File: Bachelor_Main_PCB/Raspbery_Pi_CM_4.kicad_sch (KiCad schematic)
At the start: 3 parts, among them U1 SC0683, X1 DF40HC_3.0_-100DS-0.4V_58, X2 DF40HC_3.0_-100DS-0.4V_58

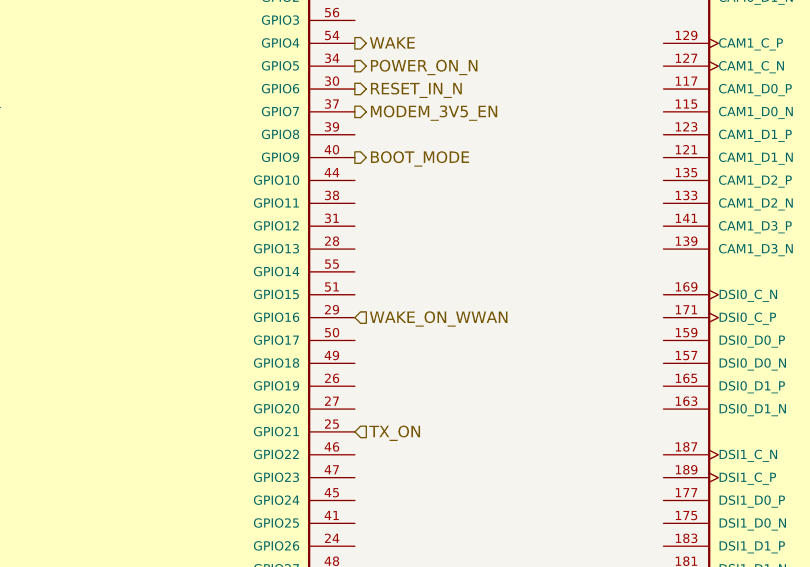
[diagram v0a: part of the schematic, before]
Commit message: Add RPI to MCU UART communication
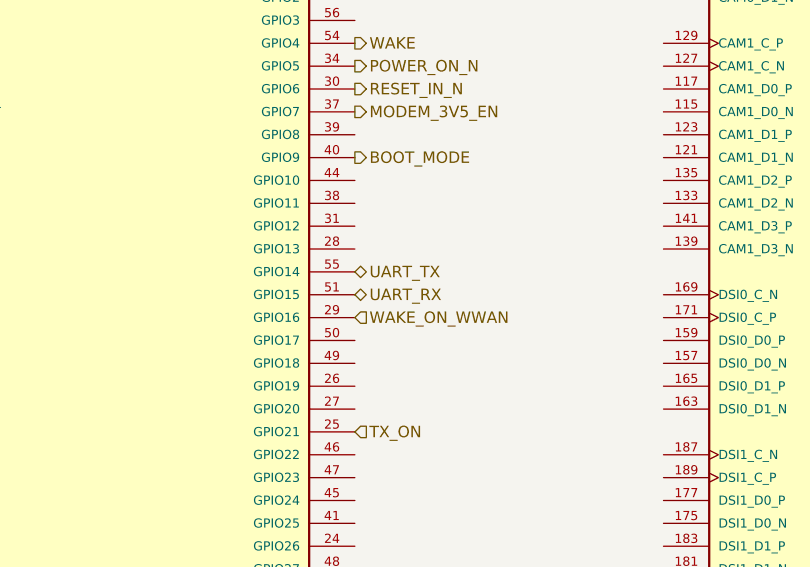
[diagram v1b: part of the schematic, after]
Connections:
- net UART_RX: now reaches U1.51 (GPIO15)
- net UART_TX: now reaches U1.55 (GPIO14)

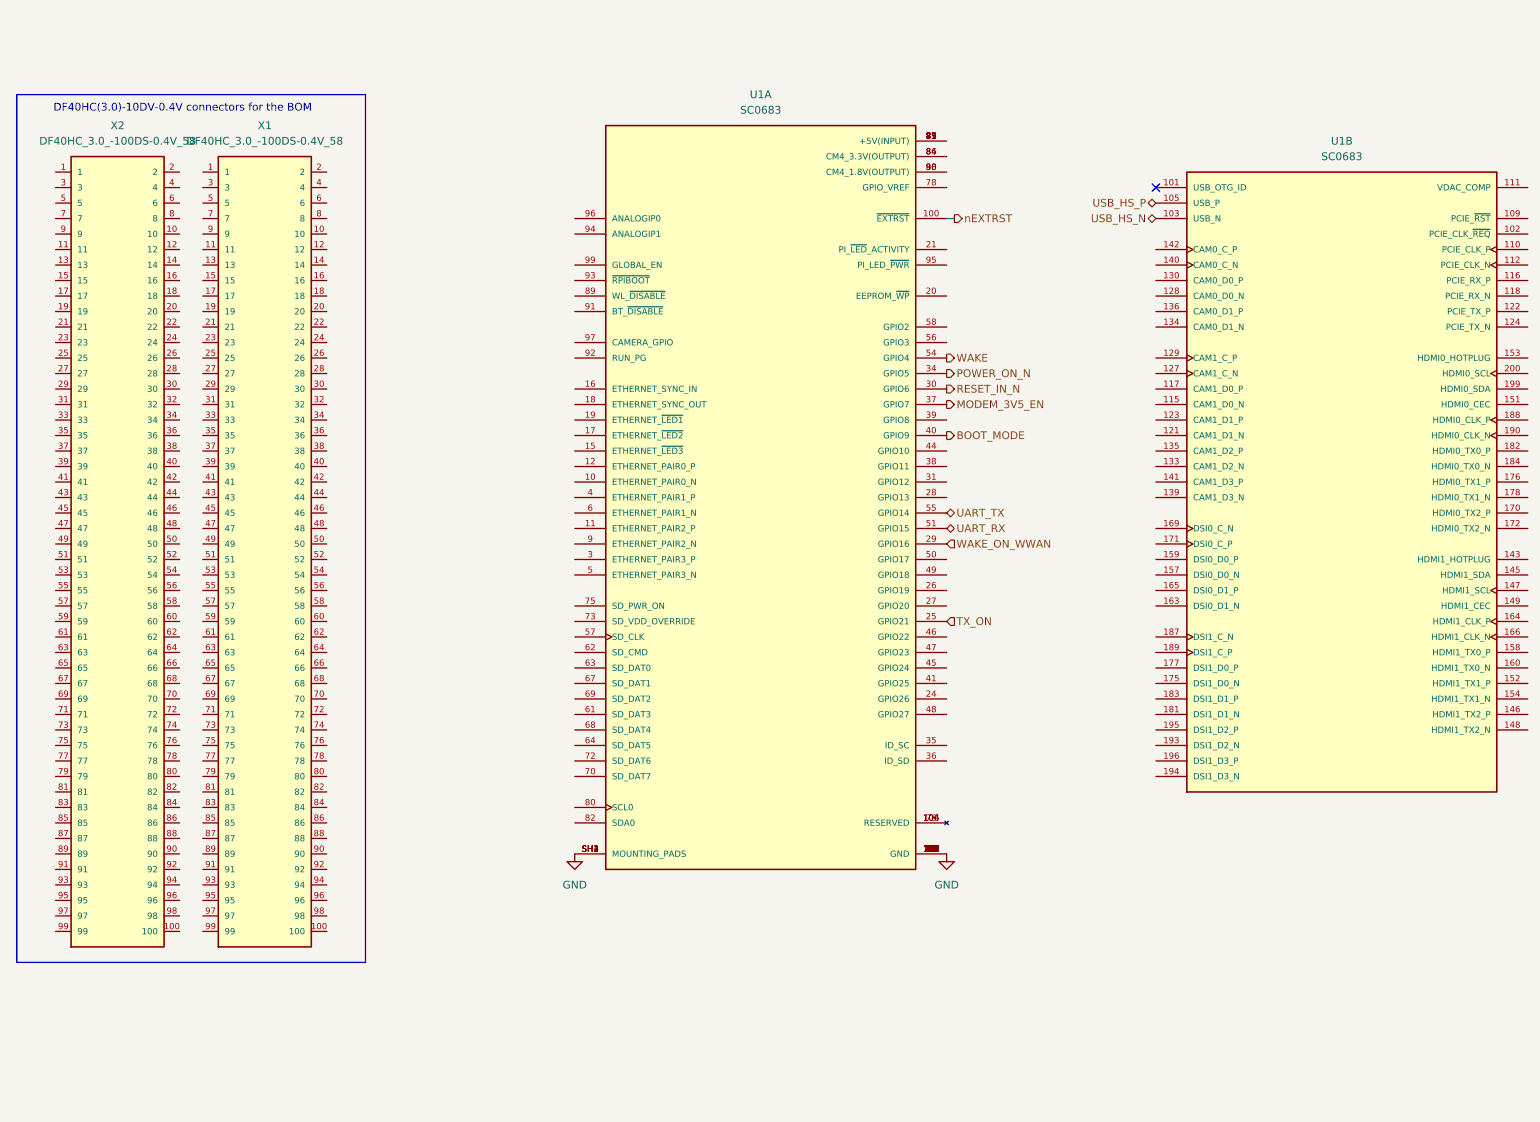
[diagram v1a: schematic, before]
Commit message: Add RPI power Switch MOSFET, Fix direction of power switch MOSFETs
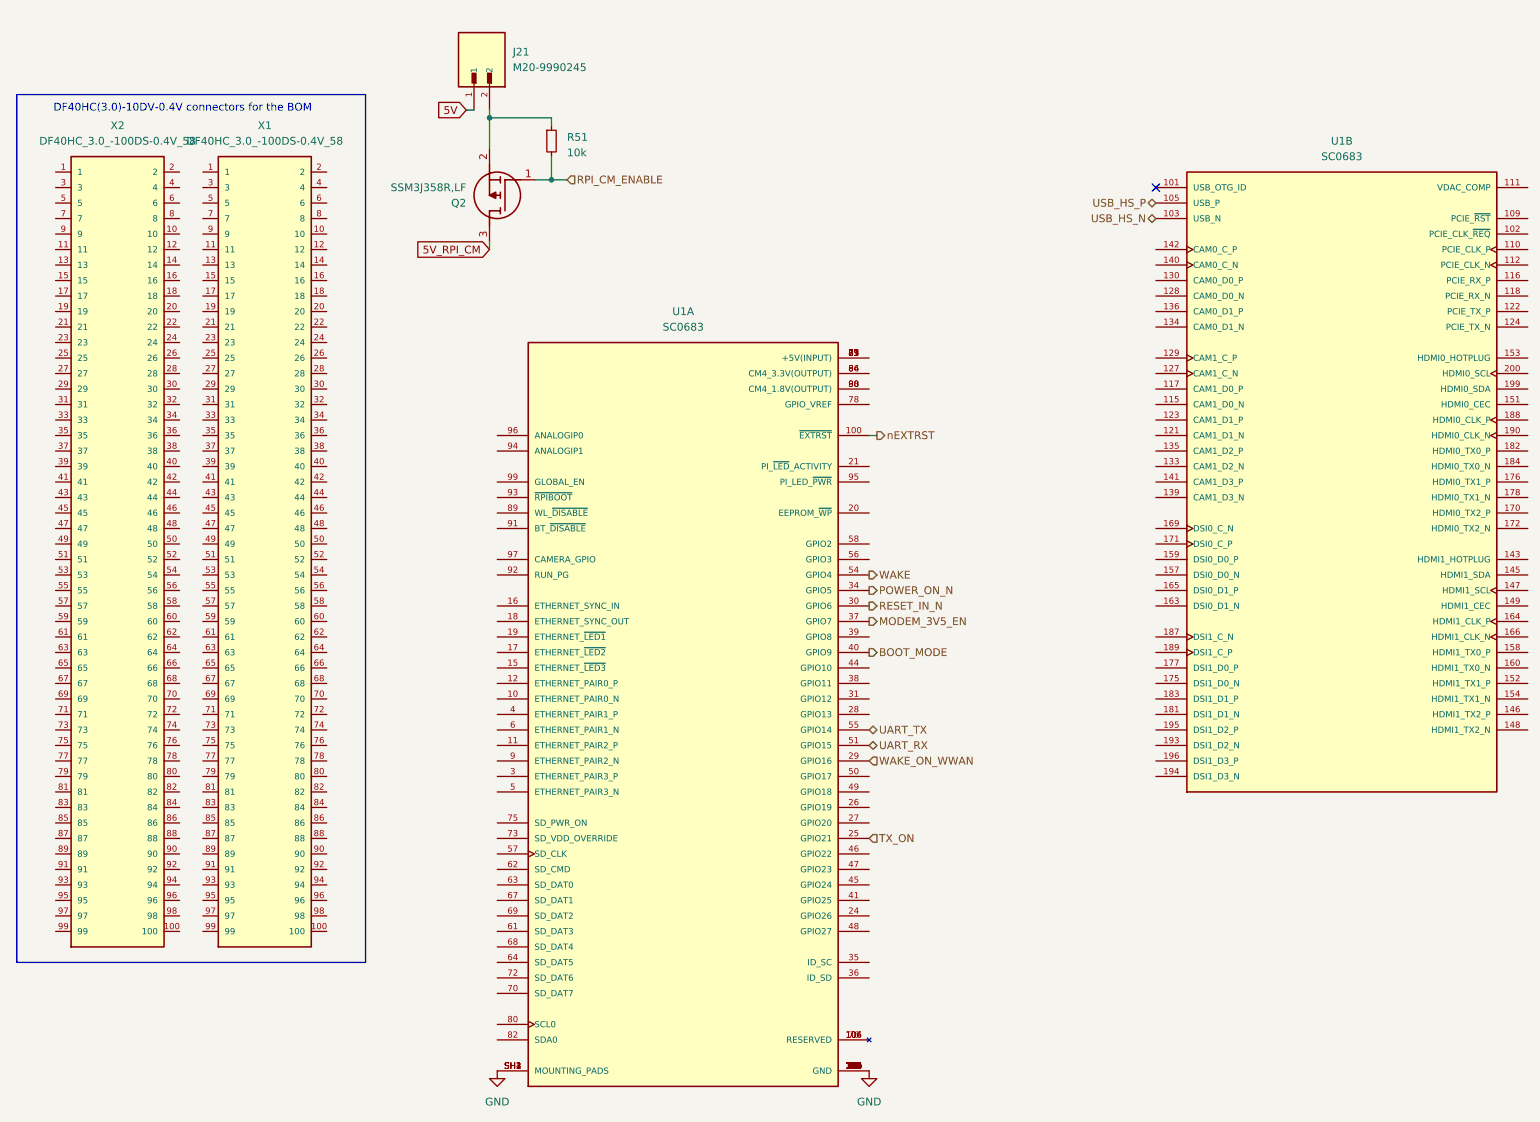
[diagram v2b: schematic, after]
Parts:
- added J21: M20-9990245, M20-9990245:HARWIN_M20-9990245, symbol M20-9990245:M20-9990245
- added Q2: SSM3J358R,LF, KiCad4:SOTFL95P240X88-3N, symbol SSM3J358R_LF:SSM3J358R,LF
- added R51: 10k, Resistor_SMD:R_0402_1005Metric, symbol Device:R_Small
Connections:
- new net: J21.2, Q2.2 (S), R51.1
- new net 5V: J21.1
- new net 5V_RPI_CM: Q2.3 (D)
- new net RPI_CM_ENABLE: Q2.1 (G), R51.2
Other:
- moved on the sheet: U1A

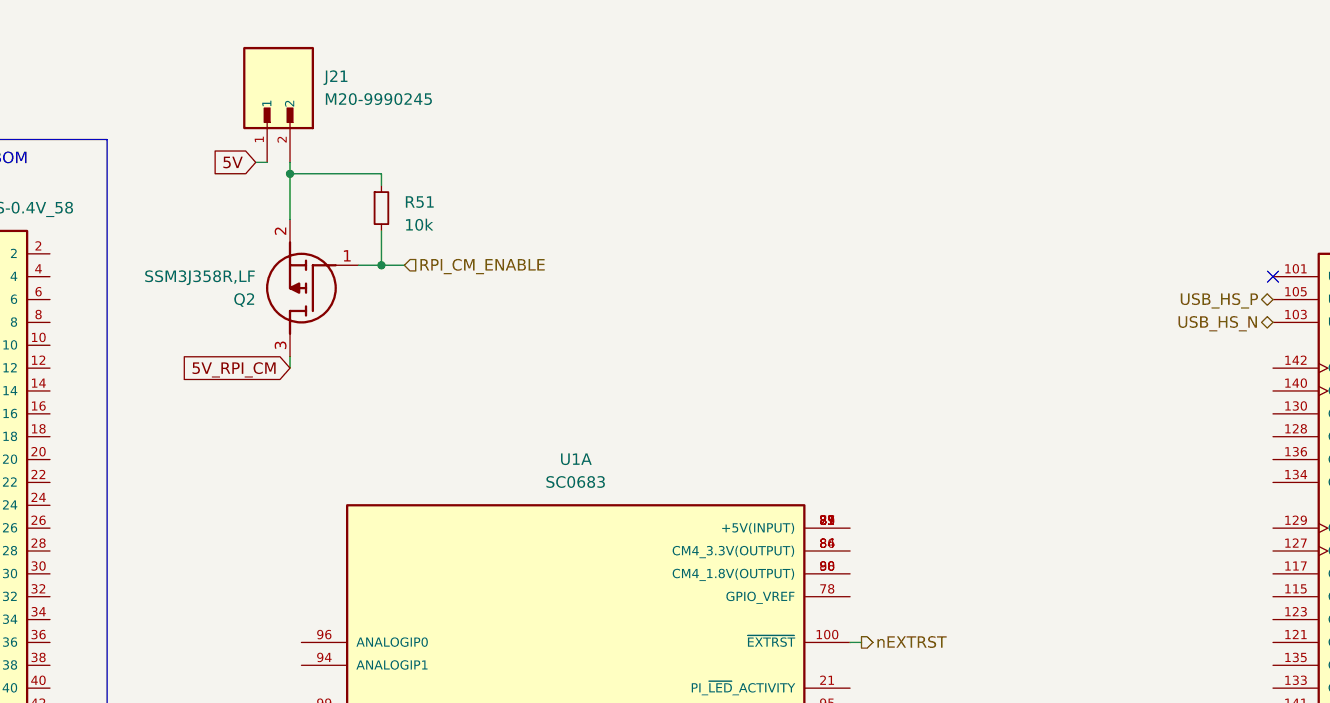
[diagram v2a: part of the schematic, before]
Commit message: Switched RX and TX for UART connection
so that the TX from RPI go into RX on MCU
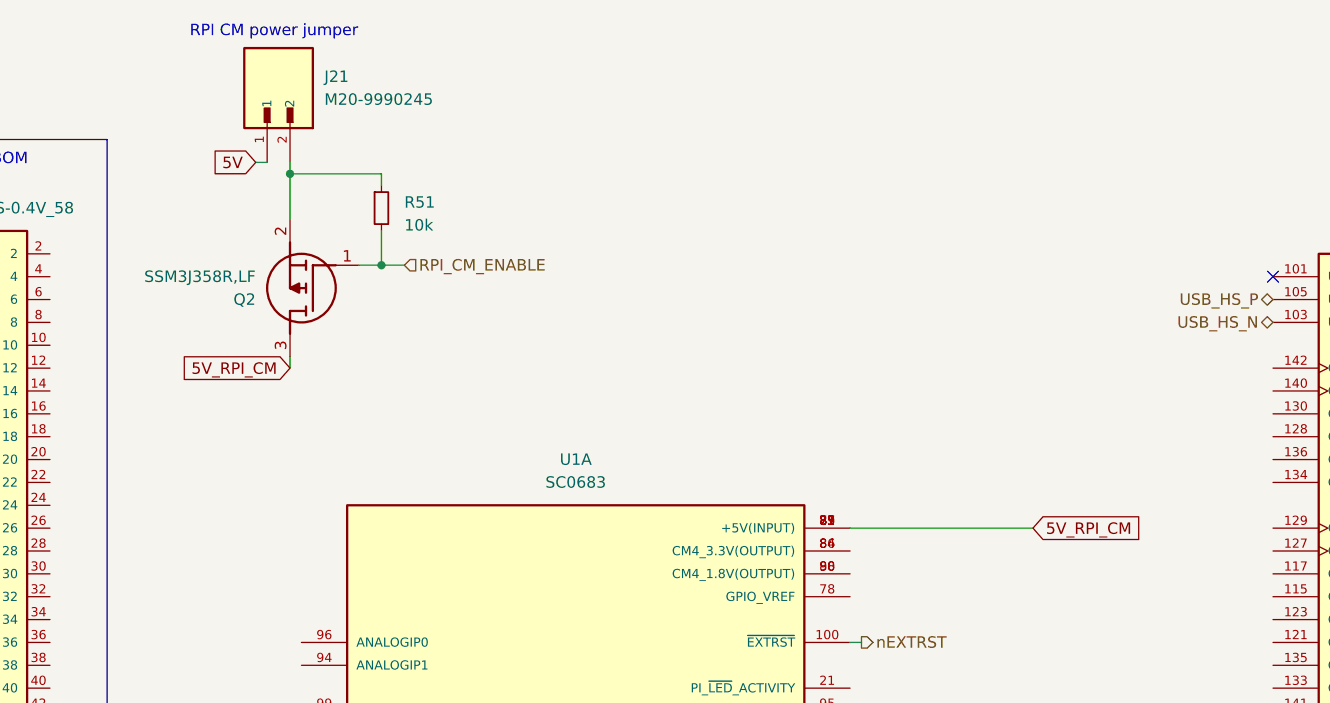
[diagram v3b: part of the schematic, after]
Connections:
- net 5V_RPI_CM: now also U1.77 (+5V(INPUT)), U1.79 (+5V(INPUT)), U1.81 (+5V(INPUT)), U1.83 (+5V(INPUT)), U1.85 (+5V(INPUT)), U1.87 (+5V(INPUT))
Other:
- note added: "RPI CM power jumper"

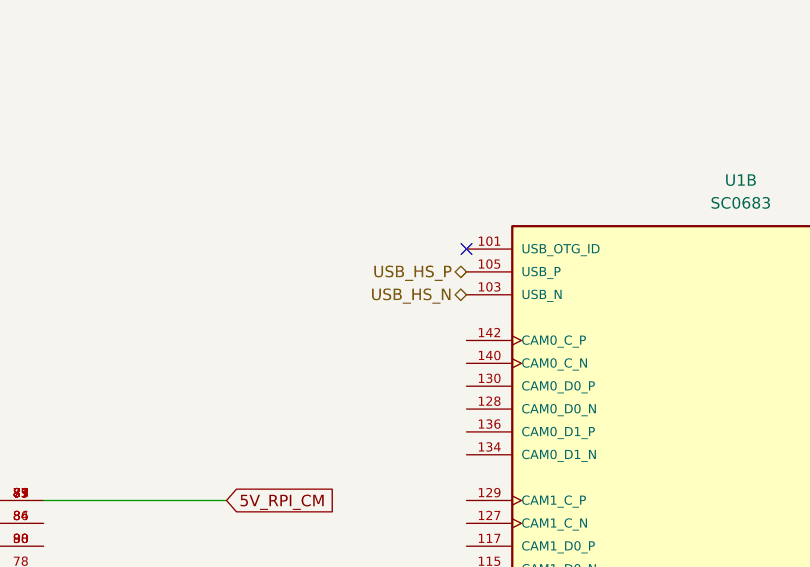
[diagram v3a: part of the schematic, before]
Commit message: Make correct stackup and add 90ohm differential pair usb
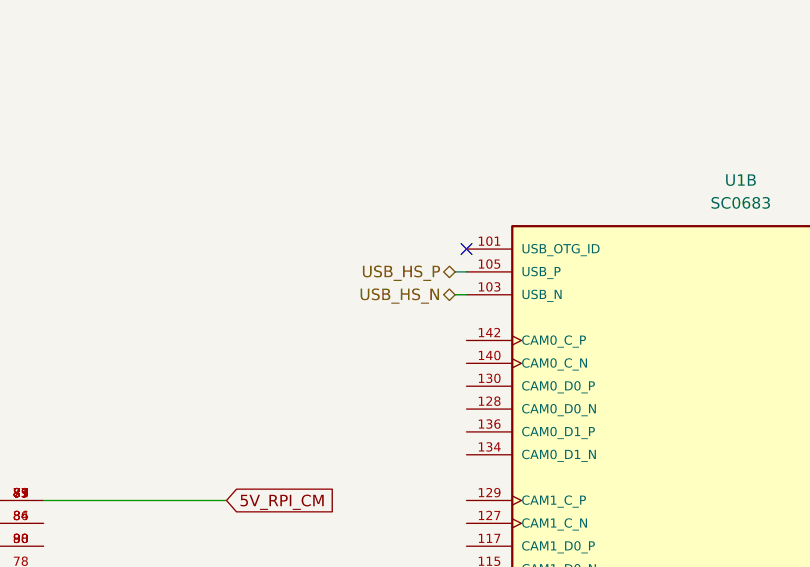
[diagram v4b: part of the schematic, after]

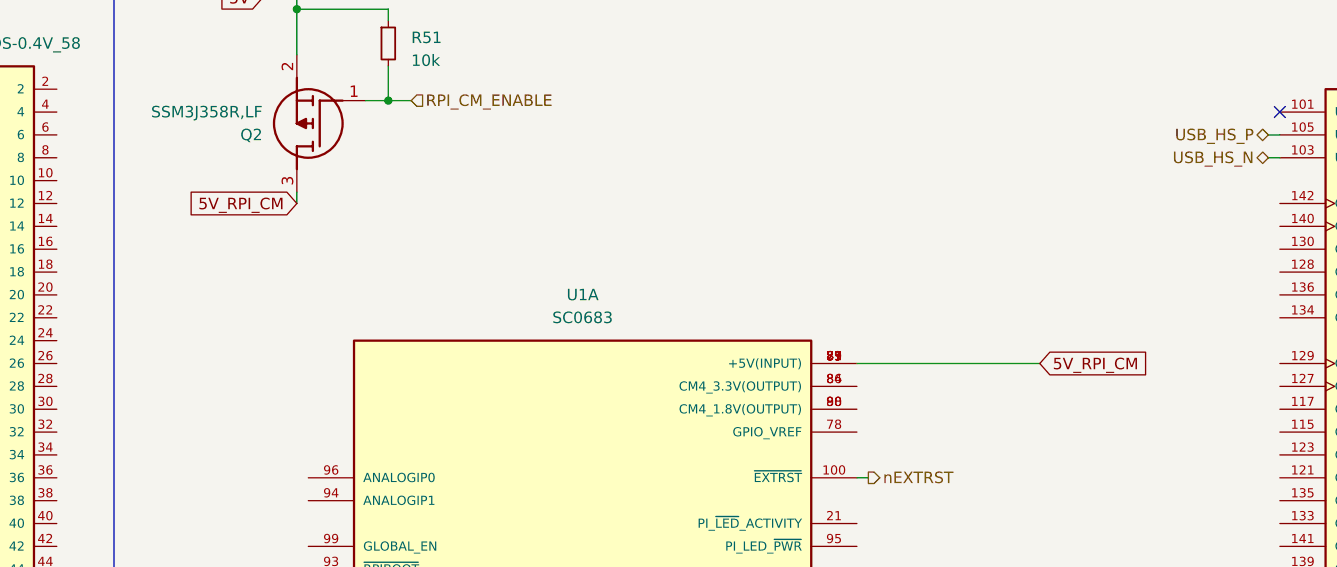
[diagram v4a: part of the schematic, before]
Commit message: Add RPI CM enable pin to MCU sheet
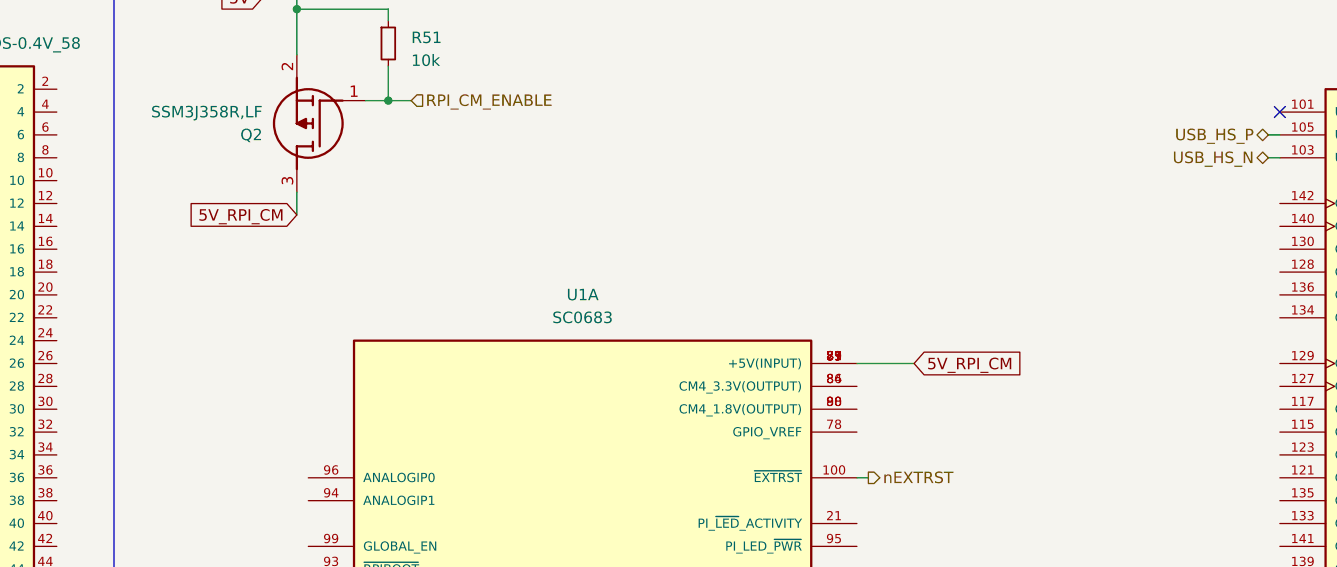
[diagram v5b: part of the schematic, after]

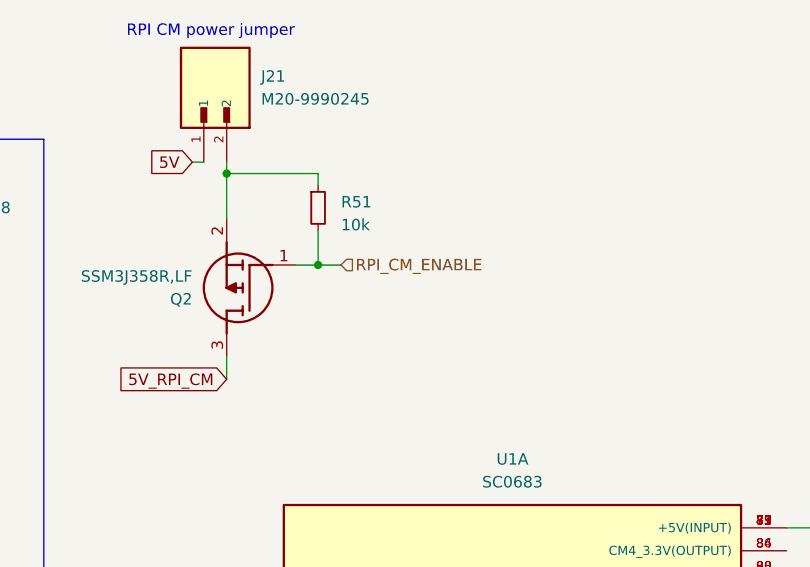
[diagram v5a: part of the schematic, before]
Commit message: Add SDcard enable VCC pin with PMOS
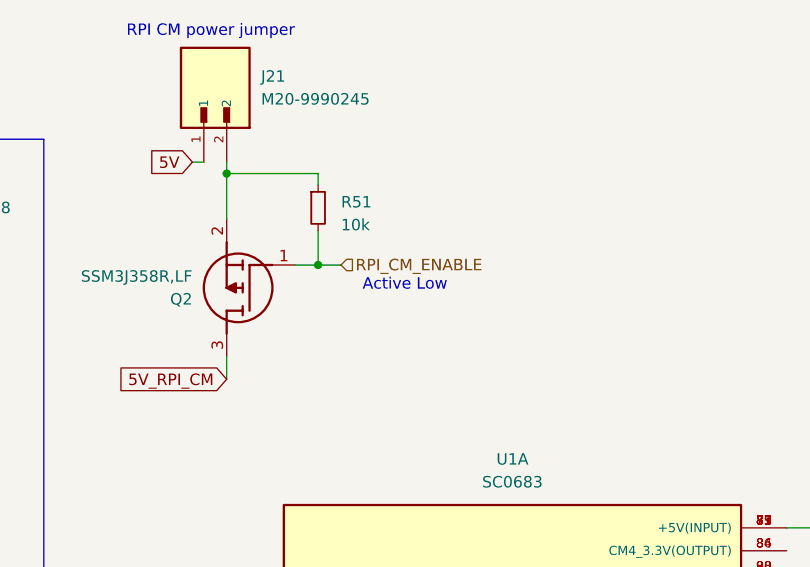
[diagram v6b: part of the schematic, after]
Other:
- note added: "Active Low"
